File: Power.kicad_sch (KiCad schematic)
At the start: 1 part

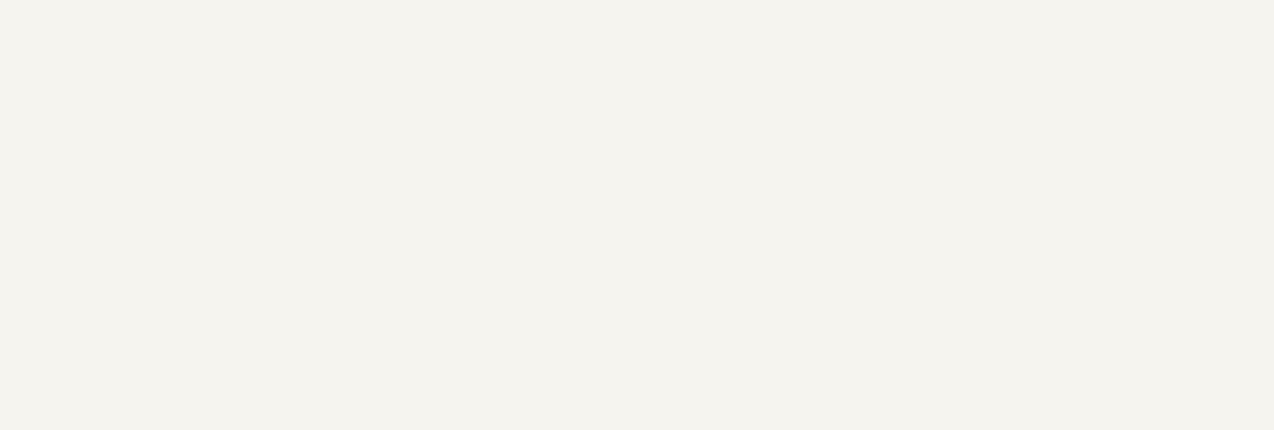
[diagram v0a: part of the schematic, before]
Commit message: 增加部分接口
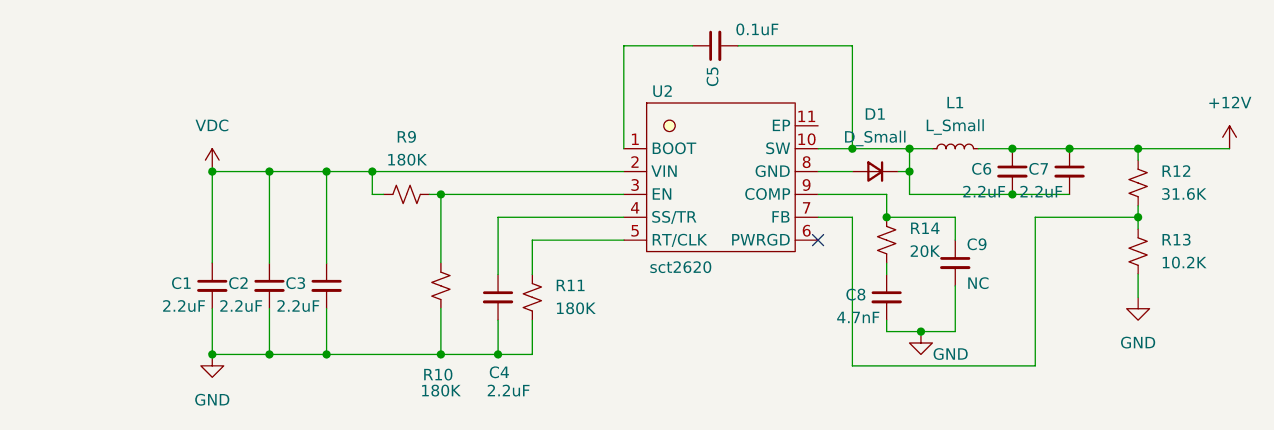
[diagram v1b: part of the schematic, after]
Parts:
- added C1, C2, C3, C4, C6, C7: 2.2uF, symbol Device:C_Small
- added C5: 0.1uF, symbol Device:C_Small
- added C8: 4.7nF, symbol Device:C_Small
- added C9: NC, symbol Device:C_Small
- added D1: D_Small, symbol Device:D_Small
- added L1: L_Small, symbol Device:L_Small
- added R10, R11, R9: 180K, symbol Device:R_Small_US
- added R12: 31.6K, symbol Device:R_Small_US
- added R13: 10.2K, symbol Device:R_Small_US
- added R14: 20K, symbol Device:R_Small_US
- added U2: sct2620, Package_SO:MSOP-10-1EP_3x3mm_P0.5mm_EP1.68x1.88mm, symbol User_Driver:SCT_2610
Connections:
- net GND: now also C1.2, C2.2, C3.2, C4.2, C8.2, C9.2, R10.1, R11.1, R13.2
- net VDC: now also C1.1, C2.1, C3.1, R9.1, U2.2 (VIN)
- new net: C5.2, C6.2, C7.2, D1.1 (K), L1.1, U2.10 (SW)
- new net: C8.1, R14.1
- new net: C9.1, R14.2, U2.9 (COMP)
- new net: R11.2, U2.5 (RT/CLK)
- new net: D1.2 (A), U2.8 (GND)
- new net: R10.2, R9.2, U2.3 (EN)
- new net: C4.1, U2.4 (SS/TR)
- new net: C5.1, U2.1 (BOOT)
- new net: R12.2, R13.1, U2.7 (FB)
- new net +12V: C6.1, C7.1, L1.2, R12.1
- no-connect marks 0 -> 1

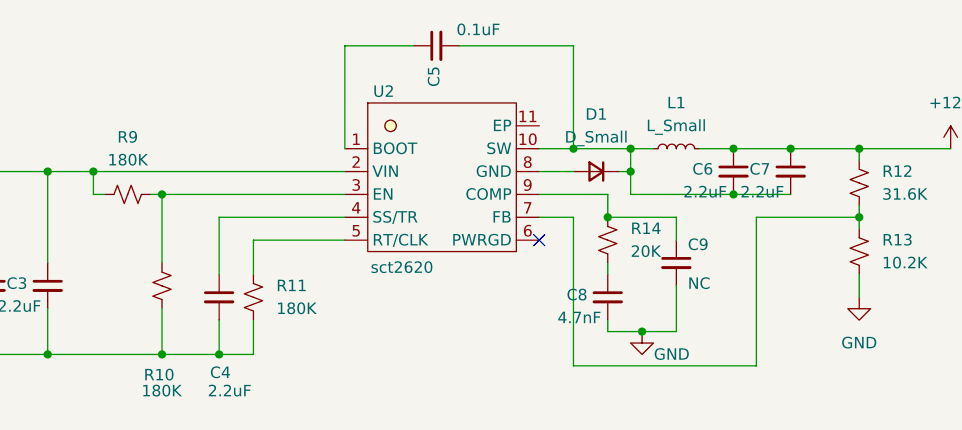
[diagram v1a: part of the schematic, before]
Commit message: 增加预驱/三相桥电路
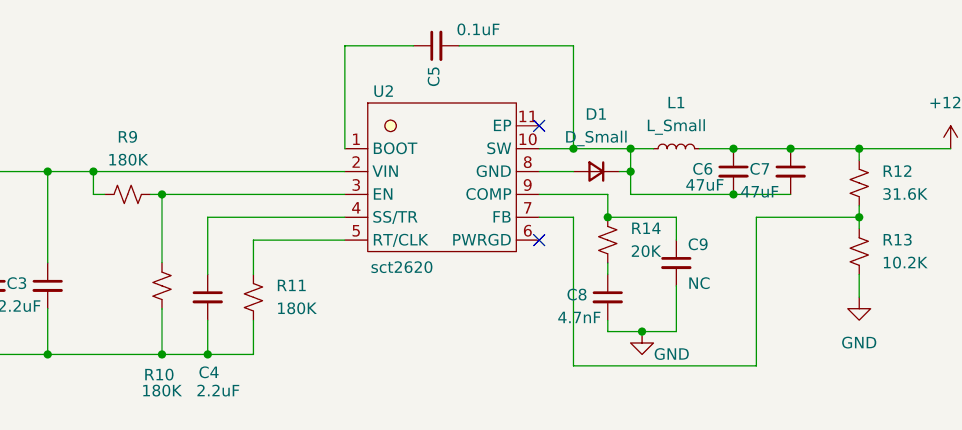
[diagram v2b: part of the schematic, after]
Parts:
- C6, C7: value 2.2uF -> 47uF
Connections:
- no-connect marks 1 -> 2
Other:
- moved on the sheet: C4

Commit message: 优化电源原理图设计
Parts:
- removed C9: NC, symbol Device:C_Small
- added C10, C11, C12: 4.7uF, symbol Device:C_Small
- added C13: 4.7nF, symbol Device:C_Small
- added C14, C17, C18: 0.1uF, symbol Device:C_Small
- added C15, C16: 47uF, symbol Device:C_Small
- added L2: 10uH, symbol Device:L_Small
- added R18: 180K, symbol Device:R_Small_US
- added R19: 43K, symbol Device:R_Small_US
- added R20: 200K, symbol Device:R_Small_US
- added R21: 53.6K, symbol Device:R_Small_US
- added R22: 10.2K, symbol Device:R_Small_US
- added R23: 20K, symbol Device:R_Small_US
- added U4: SCT2420, Package_SO:SOIC-8_5.3x6.2mm_P1.27mm, symbol User_Driver:SCT2420
- C4: value 2.2uF -> 22nF
- C8: value 4.7nF -> 1nF
- D1: value D_Small -> B360B-13-F
- L1: value L_Small -> 33uH
- R10: value 180K -> 43K
- R11: value 180K -> 200K
- R12: value 31.6K -> 143K
- R14: value 20K -> 53.6K
- U2: value sct2620 -> SCT2610
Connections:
- net +12V: now also C10.1, C11.1, C12.1, C18.1, R18.1, U4.2 (VIN)
- net GND: now also C6.2, C7.2, D1.2 (A), U2.8 (GND), C10.2, C11.2, C12.2, C13.2, C15.2, C16.2, C17.2, C18.2, R19.1, R20.1, R22.2, U4.7 (GND)
- net at C5.2, D1.1 (K), L1.1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: no longer C6.2, C7.2
- new net: R18.2, R19.2, U4.3 (EN)
- new net: C13.1, R23.1
- new net: R23.2, U4.6 (COMP)
- new net: C14.1, U4.1 (BOOT)
- new net: C14.2, L2.1, U4.8 (SW)
- new net: R20.2, U4.4 (RT/CLK)
- new net: R21.2, R22.1, U4.5 (FB)
- new net +5V: C15.1, C16.1, C17.1, L2.2, R21.1
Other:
- note added: "DC/DC 12V转5V"
- note added: "DC/DC 24V转12V"
- note added: "Vout:12V/1.5A"
- note added: "Vout:5V/2.0A"
- moved on the sheet: C1, C2, C3, C4, C6, C7, D1, L1, R10, R11, R9

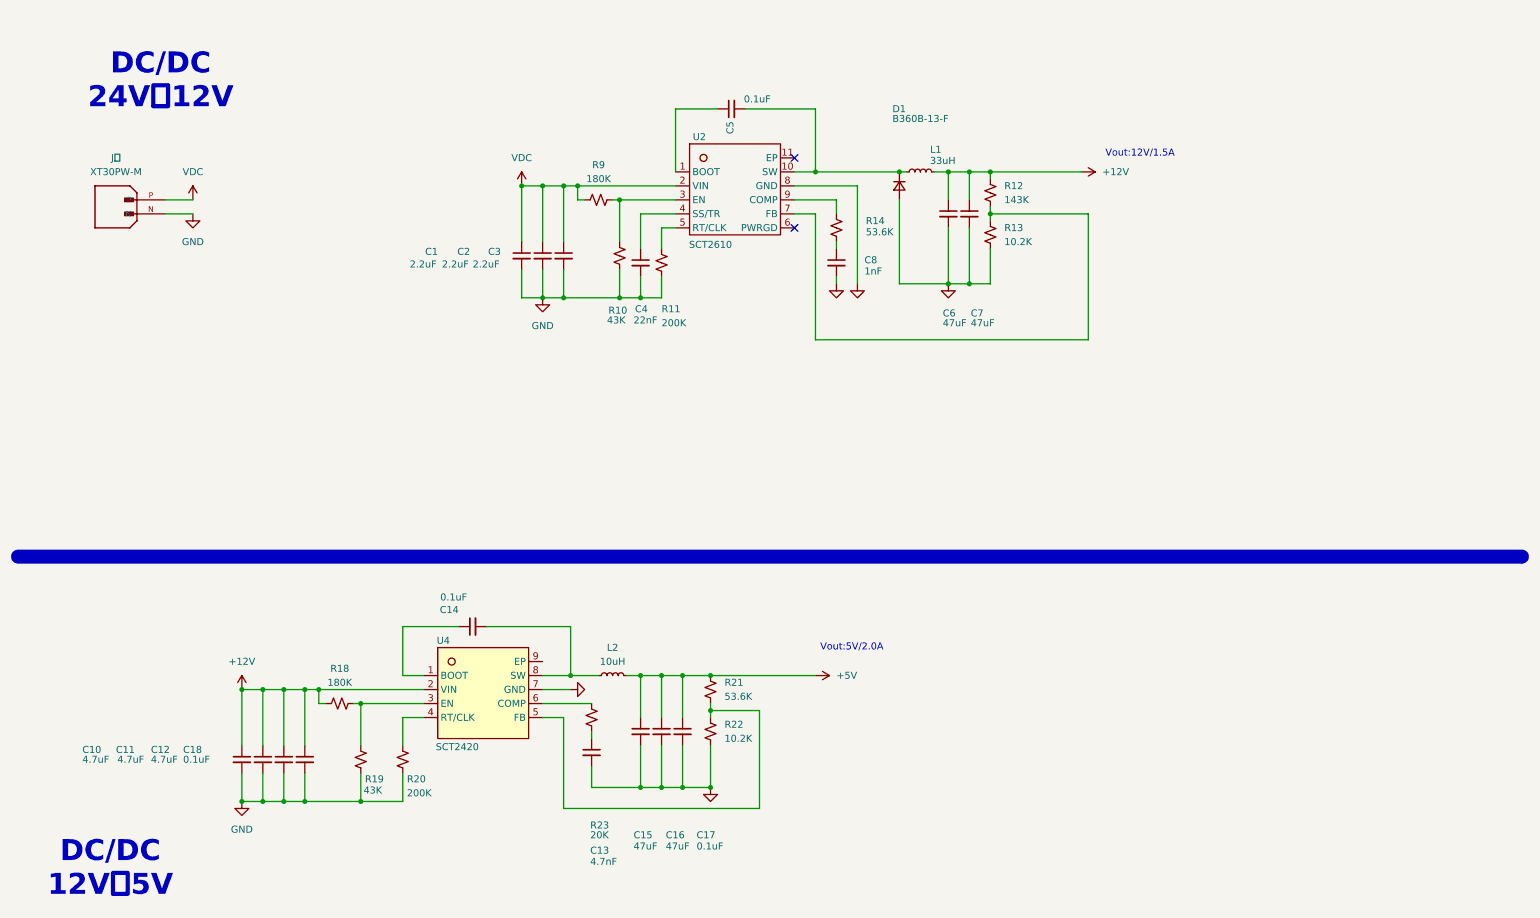
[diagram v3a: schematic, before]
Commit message: 优化5V电源/预驱电路/三相桥/运放
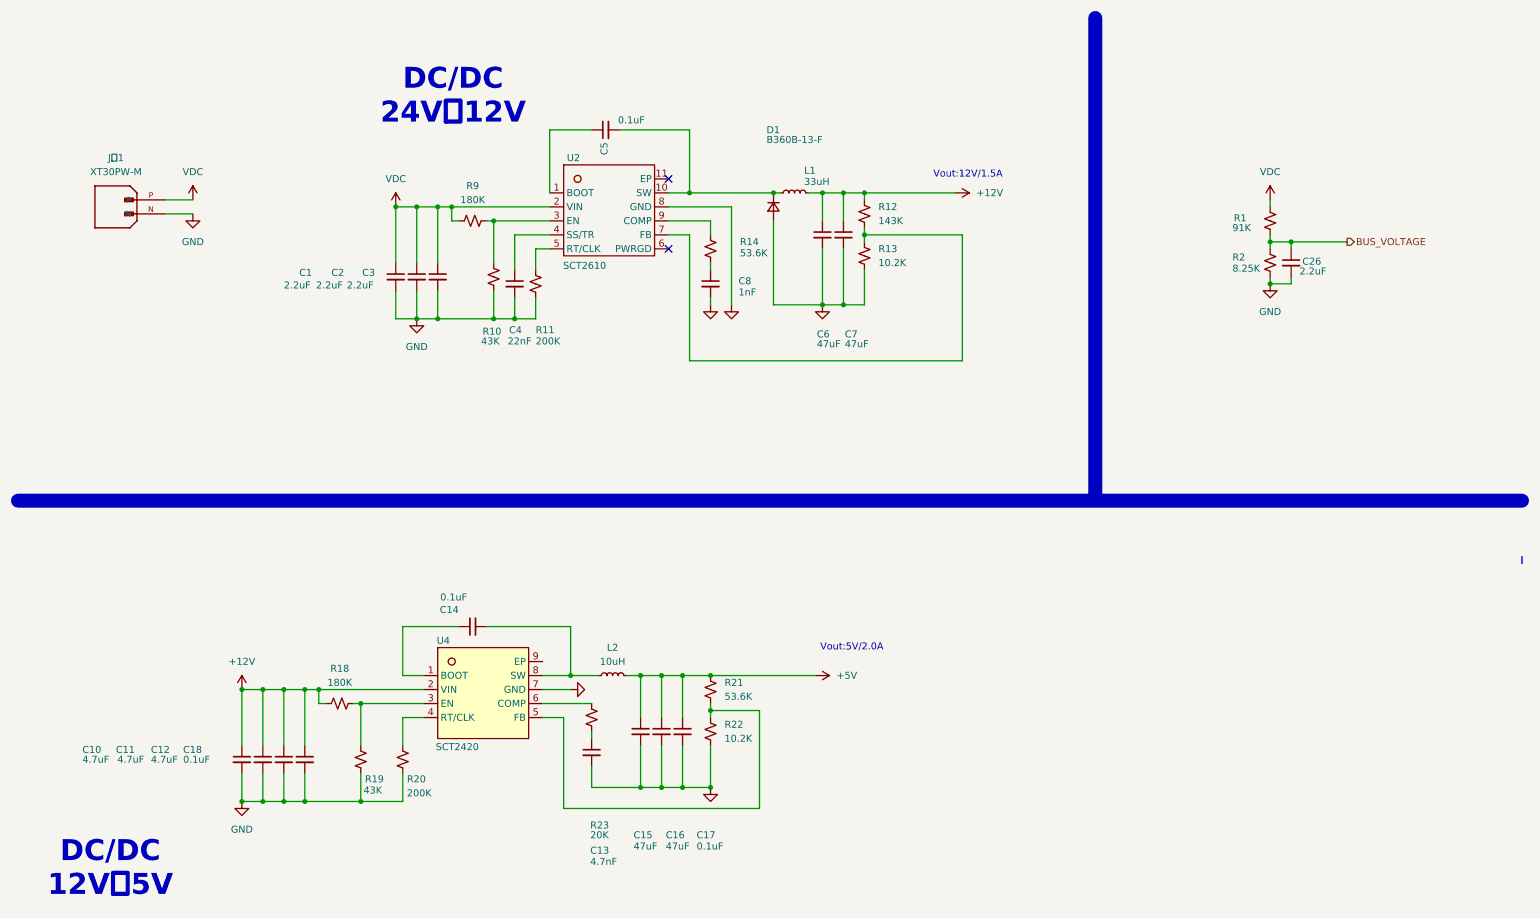
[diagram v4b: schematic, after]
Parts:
- added C26: 2.2uF, symbol Device:C_Small
- added R1: 91K, symbol Device:R_Small_US
- added R2: 8.25K, symbol Device:R_Small_US
- renumbered J？ to J？1
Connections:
- net GND: now also C26.2, R2.1
- net VDC: now also R1.2
- new net BUS_VOLTAGE: C26.1, R1.1, R2.2
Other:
- moved on the sheet: C1, C2, C3, C4, C5, C6, C7, C8, D1, L1, R10, R11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

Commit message: 分配部分封装
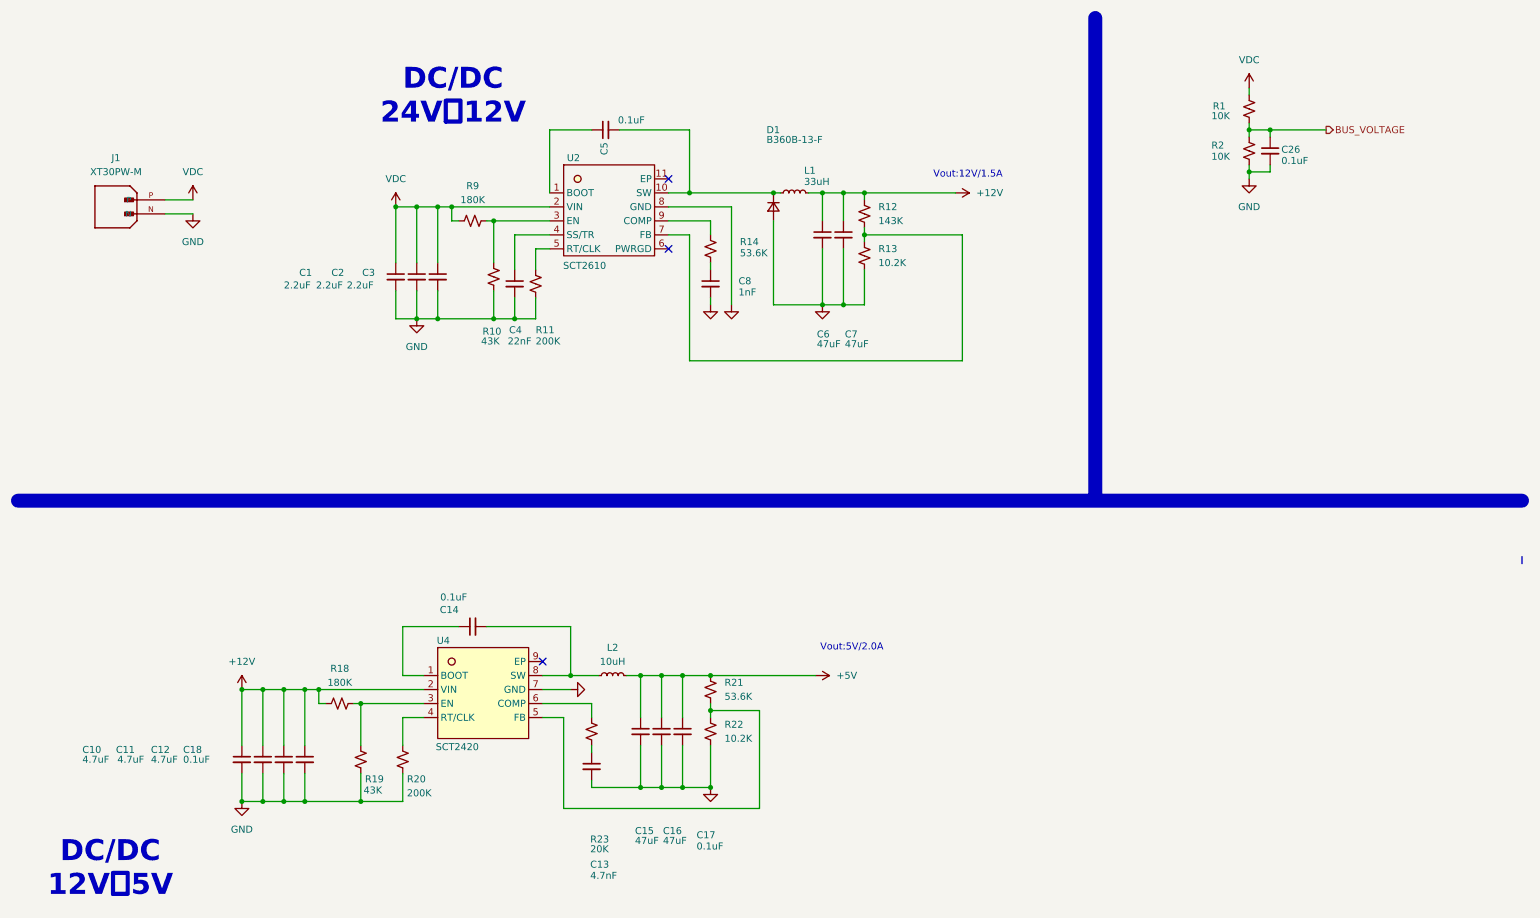
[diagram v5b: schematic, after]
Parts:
- C15, C16, C6, C7: footprint (none) -> Capacitor_SMD:C_1210_3225Metric
- C26: value 2.2uF -> 0.1uF
- D1: footprint (none) -> Diode_SMD:D_SMB
- L1, L2: footprint (none) -> Inductor_SMD:L_APV_APH0650
- R1: value 91K -> 10K
- R2: value 8.25K -> 10K
- renumbered J？1 to J1
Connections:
- no-connect marks 2 -> 3
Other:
- moved on the sheet: C13, C26, R1, R2, R23

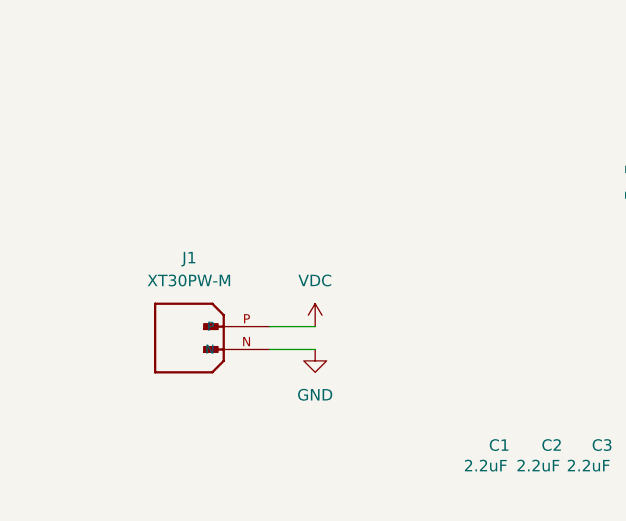
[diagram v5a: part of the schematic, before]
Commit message: 生成网表并添加到PCB
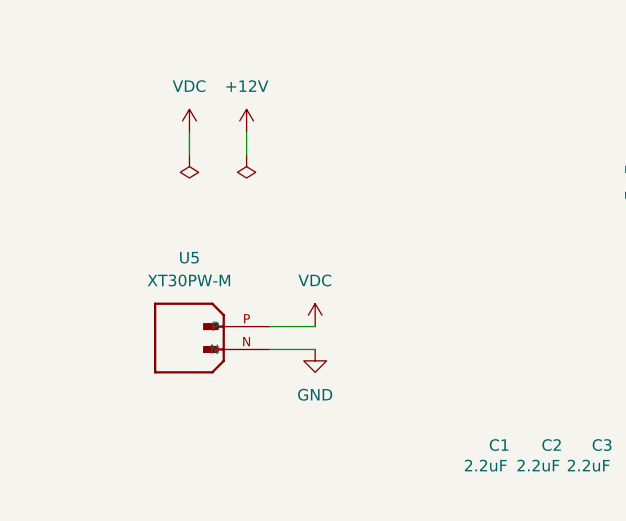
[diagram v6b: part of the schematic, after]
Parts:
- removed J1: XT30PW-M, XT30PW-M:AMASS_XT30PW-M, symbol moteus:XT30PW-M
- added U5: XT30PW-M, footprints:XT30PW-F_1x02_P2.50mm_Horizontal, symbol User_Driver:XT30PW-M
- C1, C10, C11, C12, C13, C14, C17, C18, C2, C26, C3, C4, C5, C8: footprint (none) -> Capacitor_SMD:C_0603_1608Metric
- R1, R10, R11, R12, R13, R14, R18, R19, R2, R20, R21, R22, R23, R9: footprint (none) -> Resistor_SMD:R_0603_1608Metric
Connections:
- net GND: now also U5.N
- net VDC: now also U5.P

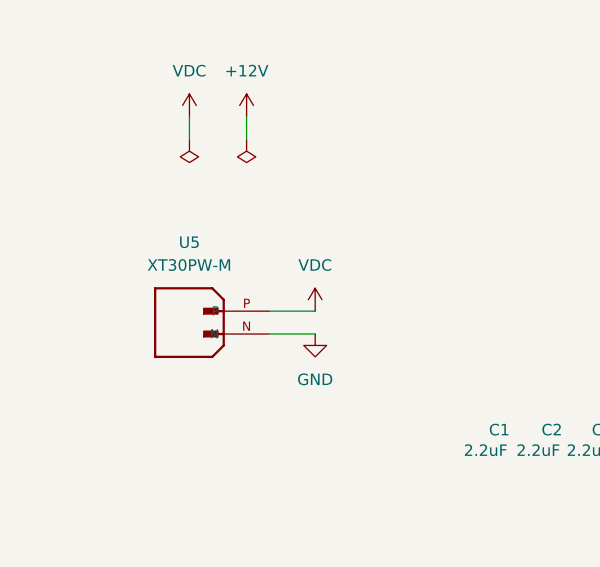
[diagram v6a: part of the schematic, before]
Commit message: 三相桥基极增加回流路径,增加VDC的输入电容
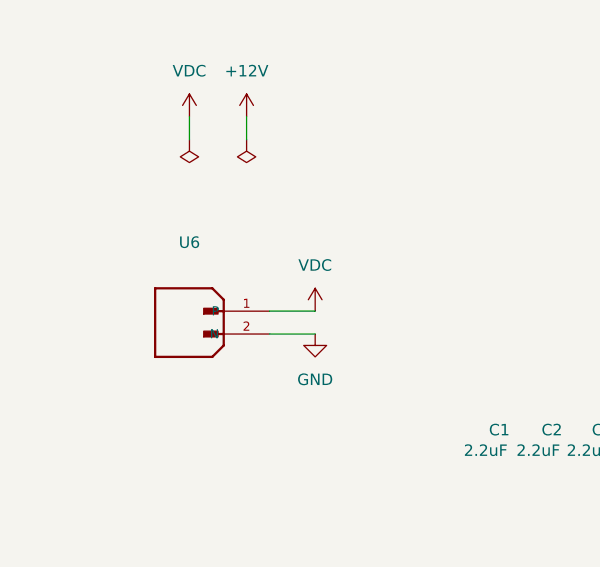
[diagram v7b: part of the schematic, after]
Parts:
- removed U5: XT30PW-M, footprints:XT30PW-F_1x02_P2.50mm_Horizontal, symbol User_Driver:XT30PW-M
- added U6: ~, footprints:XT30PW-F_1x02_P2.50mm_Horizontal, symbol User_Driver:XT30PW-M
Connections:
- net GND: now also U6.2 (N)
- net VDC: now also U6.1 (P)
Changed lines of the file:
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@@
 	)
 	(symbol
-		(lib_id "User_Driver:XT30PW-M")
-		(at 26.67 41.91 0)
-		(unit 1)
-		(exclude_from_sim no)
-		(in_bom yes)
-		(on_board yes)
-		(dnp no)
-		(fields_autoplaced yes)
-		(property "Reference" "U5"
-			(at 30.48 36.83 0)
-			(effects
-				(font
-					(size 1.27 1.27)
-				)
-			)
-		)
-		(property "Value" "XT30PW-M"
-			(at 30.48 39.37 0)
-			(effects
-				(font
-					(size 1.27 1.27)
-				)
-			)
-		)
-		(property "Footprint" "footprints:XT30PW-F_1x02_P2.50mm_Horizontal"
-			(at 26.67 41.91 0)
-			(effects
-				(font
-					(size 1.27 1.27)
-				)
-				(hide yes)
-			)
-		)
-		(property "Datasheet" ""
-			(at 26.67 41.91 0)
-			(effects
-				(font
-					(size 1.27 1.27)
-				)
-				(hide yes)
-			)
-		)
-		(property "Description" ""
-			(at 26.67 41.91 0)
-			(effects
-				(font
-					(size 1.27 1.27)
-				)
-				(hide yes)
-			)
-		)
-		(pin "P"
-		)
-		(pin "N"
-		)
-		(instances
-			(project ""
-				(path "/6b2aea6d-5084-4a15-abee-69a455b7078c/ecd3cbd5-4e2a-4cbd-93e4-e6de56463e65"
-					(reference "U5")
-					(unit 1)
-				)
-			)
-		)
-	)
-	(symbol
 		(lib_id "Device:R_Small_US")
 		(at 116.84 140.97 180)
@@
 					(unit 1)
 				)
+			)
+		)
+	)
+	(symbol
+		(lib_name "XT30PW-M_1")
+		(lib_id "User_Driver:XT30PW-M")
+		(at 26.67 41.91 0)
+		(unit 1)
+		(exclude_from_sim no)
+		(in_bom yes)
+		(on_board yes)
+		(dnp no)
+		(fields_autoplaced yes)
+		(property "Reference" "U6"
+			(at 30.48 36.83 0)
+			(effects
+				(font
+					(size 1.27 1.27)
+				)
+			)
+		)
+		(property "Value" "~"
+			(at 30.48 39.37 0)
+			(effects
+				(font
+					(size 1.27 1.27)
+				)
+			)
+		)
+		(property "Footprint" "footprints:XT30PW-F_1x02_P2.50mm_Horizontal"
+			(at 26.67 41.91 0)
+			(effects
+				(font
+					(size 1.27 1.27)
+				)
+				(hide yes)
+			)
+		)
+		(property "Datasheet" ""
+			(at 26.67 41.91 0)
+			(effects
+				(font
+					(size 1.27 1.27)
+				)
+				(hide yes)
+			)
+		)
+		(property "Description" ""
+			(at 26.67 41.91 0)
+			(effects
+				(font
+					(size 1.27 1.27)
+				)
+				(hide yes)
+			)
+		)
+		(pin "1"
+		)
+		(pin "2"
+		)
+		(instances
+			(project ""
+				(path "/6b2aea6d-5084-4a15-abee-69a455b7078c/ecd3cbd5-4e2a-4cbd-93e4-e6de56463e65"
+					(reference "U6")
+					(unit 1)
+				)

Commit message: 优化原理图
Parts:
- added C8: 2.2uF, Capacitor_SMD:C_0603_1608Metric, symbol Device:C_Small
- renumbered C10 to C1, C4 to C10, C13 to C11, C5 to C12, C15 to C13, C16 to C14, C17 to C15, C8 to C16, C6 to C17, C7 to C18, C26 to C19, C11 to C2, C12 to C3, C18 to C4, C1 to C5, C2 to C6, C3 to C7, C14 to C9, L2 to L1, L1 to L2, R18 to R1, R22 to R10, R12 to R11, R13 to R12, R1 to R13, R2 to R14, R19 to R2, R20 to R3, R9 to R4, R10 to R5, R11 to R6, R23 to R7, R14 to R8, R21 to R9, U6 to U1, U4 to U2, U2 to U3
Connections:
- net GND: now also C8.2
- net VDC: now also C8.1
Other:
- moved on the sheet: C10, C5, C6, C7, R4, R5, R6
